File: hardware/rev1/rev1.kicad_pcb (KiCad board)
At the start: 2 copper layers, 26 parts, among them U1 BNO055, U2 MPL3115A2, U3 Teensy3.6, Y1 Crystal_32kHz768

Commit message: wip
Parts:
- moved Y1 168.0 mm to (132.1, 140.7), turned to 90 degrees
- moved C1 166.6 mm to (132.6, 146.4)
- moved C2 165.9 mm to (132.6, 142.6), turned to 180 degrees
- moved C3 164.3 mm to (132.6, 144.5), turned to 180 degrees
- moved C5 157.1 mm to (135.3, 140.6)
- moved R2 155.9 mm to (128.3, 143.4), turned to 180 degrees
- moved R3 155.0 mm to (131.6, 135.6), turned to 180 degrees
- moved C4 154.7 mm to (125.6, 141.6), turned to 270 degrees
- moved C6 152.6 mm to (135.3, 138.4)
- moved TP6 151.5 mm to (124.2, 135.8)
- moved R1 147.6 mm to (125.0, 138.7)
- moved R4 144.7 mm to (128.3, 135.6)
- moved TP_GND1 143.5 mm to (120.7, 135.6)
- moved TP7 143.2 mm to (116.6, 135.6)
- moved TP3 138.9 mm to (122.8, 141.7)
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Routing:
- net OptionalOSCoutput: track 0.00 -> 3.06 mm
- net OptionalOSCinput: track 0.00 -> 1.88 mm
- net VDD: track 0.00 -> 1.63 mm

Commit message: wip
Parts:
- added TP10: TestPoint, footprints:Test_Point_D1.02mm, F.Cu at (135.4, 135.5)
- added TP9: TestPoint, footprints:Test_Point_D1.02mm, F.Cu at (136.2, 143.2)
- moved TP6 4.32 mm to (119.9, 135.6)
- moved TP_GND1 4.25 mm to (116.4, 135.6)
- moved TP7 3.75 mm to (112.8, 135.6)
- moved TP3 0.40 mm to (122.9, 141.3)
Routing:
- net GND: track 0.00 -> 19.0 mm
- net nBOOT_LOAD_PIN: track 0.00 -> 15.9 mm, vias 0 -> 1
- net nRESET: track 0.00 -> 6.56 mm, vias 0 -> 1
- net VDD: track 1.63 -> 7.65 mm
- net OptionalOSCoutput: track 3.06 -> 8.73 mm
- net OptionalOSCinput: track 1.88 -> 7.52 mm
- net Net-(C4-Pad1): track 0.00 -> 4.58 mm
- net INT_BNO055: track 0.00 -> 4.49 mm, vias 0 -> 1

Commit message: wip (slick)
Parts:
- moved R3 0.97 mm to (131.8, 134.7)
- moved R4 0.96 mm to (128.4, 134.7)
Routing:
- net VDD: track 7.65 -> 32.7 mm, vias 0 -> 3
- net COM3: track 0.00 -> 5.26 mm, vias 0 -> 1
- net SDA_TEENSY: track 0.00 -> 5.03 mm
- net SCL_TEENSY: track 0.00 -> 4.72 mm
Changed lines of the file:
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@@
     (thickness 1.6)
     (drawings 0)
-    (tracks 73)
+    (tracks 107)
     (zones 0)
     (modules 28)
@@
   )
   (module footprints:R_0805_OEM (layer F.Cu)
-    (at 131.572 135.636 180)
+    (at 131.7625 134.6835 180)
     (descr "Resistor SMD 0805, reflow soldering, Vishay (see dcrcw.pdf)")
     (tags "resistor 0805")
@@
   )
   (module footprints:R_0805_OEM (layer F.Cu)
-    (at 128.27 135.636)
+    (at 128.397 134.6835)
     (descr "Resistor SMD 0805, reflow soldering, Vishay (see dcrcw.pdf)")
     (tags "resistor 0805")
@@
   (segment (start 129.22 143.1265) (end 128.906 142.8125) (width 0.25) (layer F.Cu) (net 2) (status C00000))
   (segment (start 128.906 142.8125) (end 128.906 141.8185) (width 0.25) (layer F.Cu) (net 2) (status C00000))
+  (segment (start 127.447 134.6835) (end 127.447 136.078) (width 0.25) (layer F.Cu) (net 2) (status 400000))
+  (segment (start 127.3175 137.287) (end 130.3655 140.335) (width 0.25) (layer B.Cu) (net 2))
+  (segment (start 127.3175 137.16) (end 127.3175 137.287) (width 0.25) (layer B.Cu) (net 2))
+  (segment (start 127.447 136.078) (end 127.3175 136.2075) (width 0.25) (layer F.Cu) (net 2))
+  (via (at 127.3175 136.2075) (size 0.8) (drill 0.4) (layers F.Cu B.Cu) (net 2))
+  (segment (start 127.3175 136.2075) (end 127.3175 137.16) (width 0.25) (layer B.Cu) (net 2))
+  (segment (start 132.7125 134.6835) (end 132.7125 134.8765) (width 0.25) (layer F.Cu) (net 2) (status C00000))
+  (segment (start 130.3655 139.319) (end 130.3655 137.2235) (width 0.25) (layer B.Cu) (net 2))
+  (segment (start 130.3655 142.748) (end 130.3655 140.335) (width 0.25) (layer B.Cu) (net 2))
+  (segment (start 130.3655 140.335) (end 130.3655 139.319) (width 0.25) (layer B.Cu) (net 2))
+  (via (at 130.3655 142.748) (size 0.8) (drill 0.4) (layers F.Cu B.Cu) (net 2))
+  (segment (start 129.7305 142.748) (end 130.3655 142.748) (width 0.25) (layer F.Cu) (net 2))
+  (segment (start 129.22 143.2585) (end 129.7305 142.748) (width 0.25) (layer F.Cu) (net 2) (status 400000))
+  (segment (start 129.22 143.2585) (end 129.22 143.383) (width 0.25) (layer F.Cu) (net 2) (status C00000))
+  (segment (start 132.7125 134.8765) (end 131.3815 136.2075) (width 0.25) (layer F.Cu) (net 2) (status 400000))
+  (via (at 131.3815 136.2075) (size 0.8) (drill 0.4) (layers F.Cu B.Cu) (net 2))
+  (segment (start 131.3815 136.2075) (end 130.3655 137.2235) (width 0.25) (layer B.Cu) (net 2))
+  (segment (start 124.018 138.684) (end 124.018 136.586) (width 0.25) (layer F.Cu) (net 2) (status 400000))
+  (segment (start 125.9205 134.6835) (end 127.447 134.6835) (width 0.25) (layer F.Cu) (net 2) (status 800000))
+  (segment (start 124.018 136.586) (end 125.9205 134.6835) (width 0.25) (layer F.Cu) (net 2))
+  (segment (start 130.3655 142.748) (end 131.461 142.748) (width 0.25) (layer F.Cu) (net 2) (status 800000))
+  (segment (start 131.461 142.748) (end 131.588 142.621) (width 0.25) (layer F.Cu) (net 2) (status C00000))
   (segment (start 127.0935 140.256) (end 125.952 140.256) (width 0.25) (layer F.Cu) (net 3) (status C00000))
   (segment (start 125.952 140.256) (end 125.603 140.605) (width 0.25) (layer F.Cu) (net 3) (status C00000))
@@
   (segment (start 124.206 142.748) (end 124.9045 142.0495) (width 0.25) (layer B.Cu) (net 8))
   (segment (start 124.9045 142.0495) (end 124.9045 139.7635) (width 0.25) (layer B.Cu) (net 8))
+  (segment (start 130.2185 137.256) (end 130.2185 135.2775) (width 0.25) (layer F.Cu) (net 9) (status 400000))
+  (segment (start 130.2185 135.2775) (end 130.8125 134.6835) (width 0.25) (layer F.Cu) (net 9) (status 800000))
+  (segment (start 130.8125 134.6835) (end 130.8125 132.649) (width 0.25) (layer F.Cu) (net 9) (status 400000))
+  (segment (start 130.8125 132.649) (end 130.937 132.5245) (width 0.25) (layer F.Cu) (net 9))
+  (segment (start 129.406 137.1935) (end 129.406 134.7425) (width 0.25) (layer F.Cu) (net 10) (status C00000))
+  (segment (start 129.406 134.7425) (end 129.347 134.6835) (width 0.25) (layer F.Cu) (net 10) (status C00000))
+  (segment (start 129.347 134.6835) (end 129.347 132.5855) (width 0.25) (layer F.Cu) (net 10) (status 400000))
+  (segment (start 129.347 132.5855) (end 129.286 132.5245) (width 0.25) (layer F.Cu) (net 10))
+  (segment (start 128.406 137.1935) (end 128.406 136.262) (width 0.25) (layer F.Cu) (net 13) (status 400000))
+  (segment (start 128.4605 136.2075) (end 128.4605 131.953) (width 0.25) (layer B.Cu) (net 13))
+  (via (at 128.4605 136.2075) (size 0.8) (drill 0.4) (layers F.Cu B.Cu) (net 13))
+  (segment (start 128.406 136.262) (end 128.4605 136.2075) (width 0.25) (layer F.Cu) (net 13))
   (segment (start 127.0935 137.756) (end 126.7705 137.756) (width 0.25) (layer F.Cu) (net 14) (status 400000))
   (segment (start 126.111 137.0965) (end 126.111 133.858) (width 0.25) (layer B.Cu) (net 14))

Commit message: wip
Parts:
- moved R2 1.38 mm to (128.3, 144.8)
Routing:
- net GND: track 19.0 -> 60.3 mm, vias 0 -> 6
- net VDD: track 32.7 -> 40.6 mm
- net INT_BNO055: track 4.49 -> 1.26 mm
- net nBOOT_LOAD_PIN: track 15.9 -> 17.2 mm

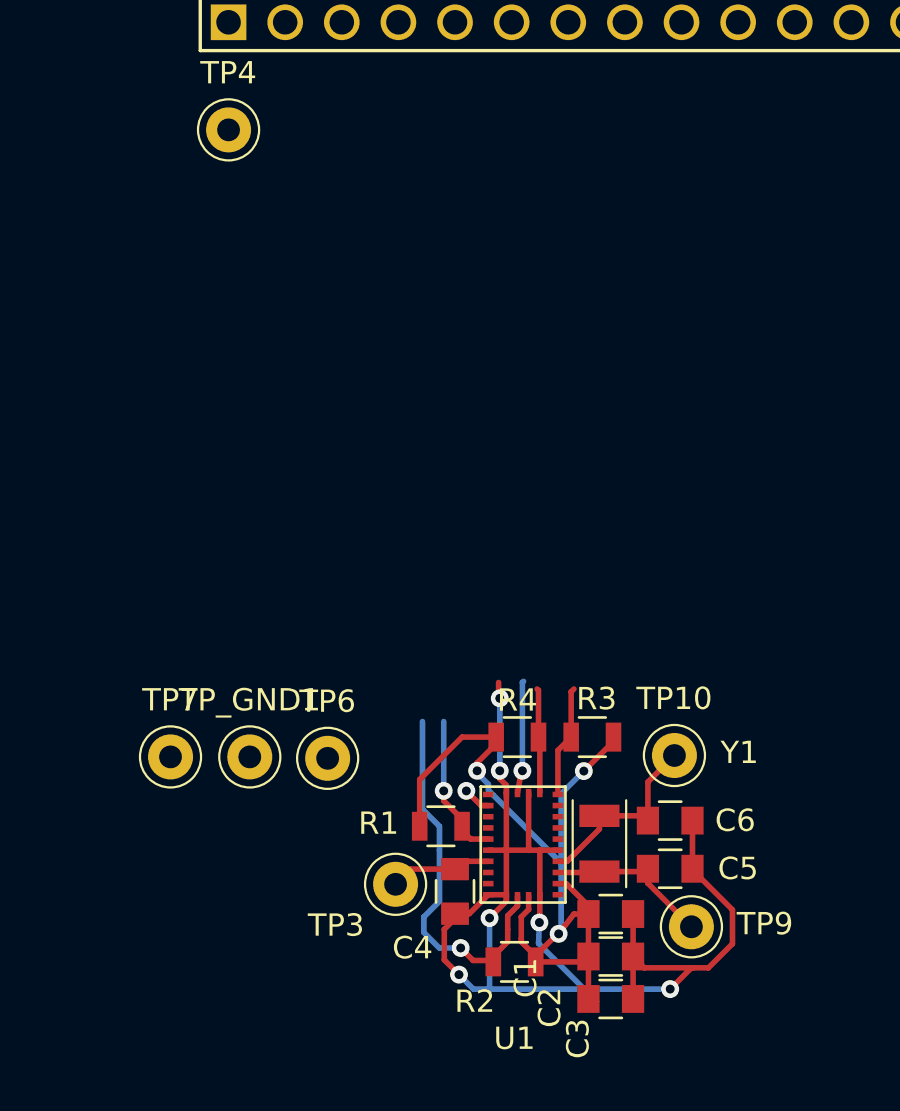
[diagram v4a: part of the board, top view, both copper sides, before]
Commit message: finish BNO055 portion of layout
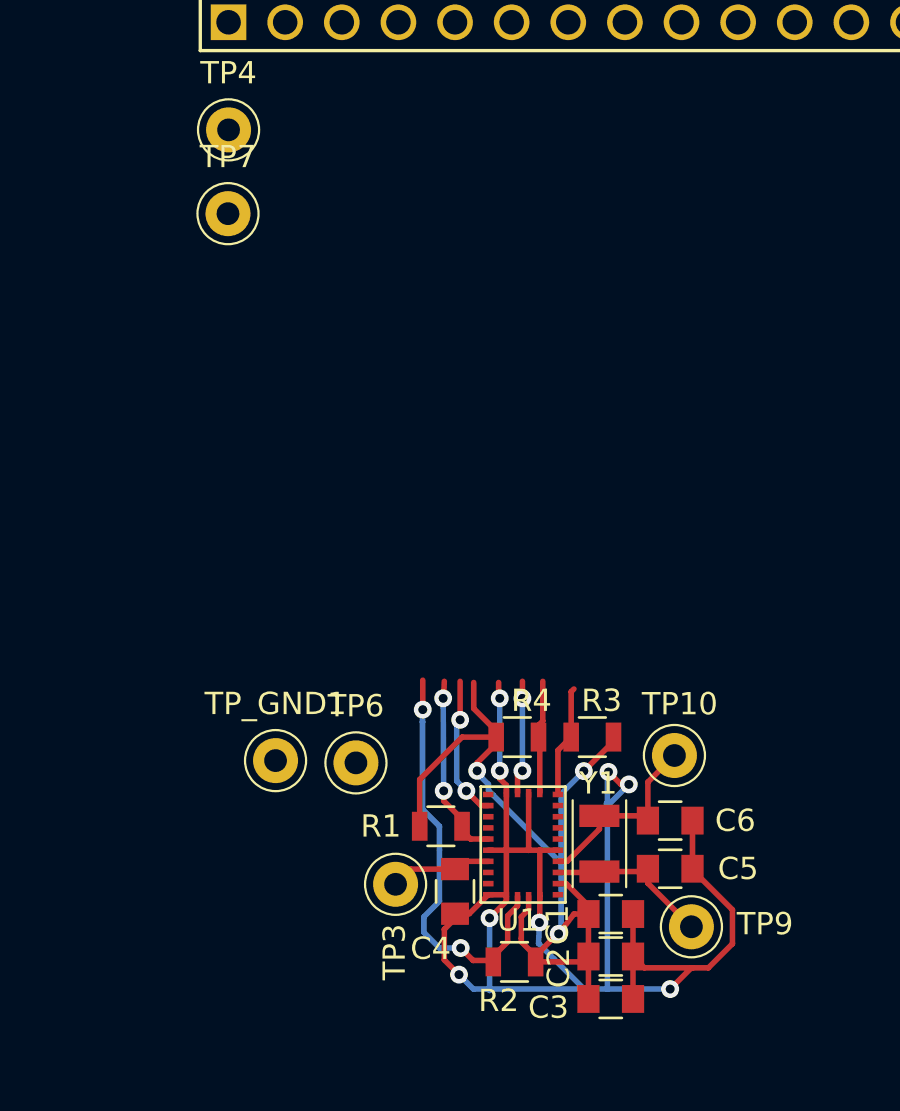
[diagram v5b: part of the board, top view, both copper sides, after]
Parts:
- moved TP7 24.5 mm to (115.4, 111.2)
- moved TP6 1.29 mm to (121.2, 135.8)
- moved TP_GND1 1.17 mm to (117.6, 135.7)
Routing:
- net GND: track 60.3 -> 72.3 mm, vias 6 -> 8
- net INT_BNO055: track 1.26 -> 6.41 mm, vias 1 -> 2
- net VDD: track 40.6 -> 43.5 mm
- net nBOOT_LOAD_PIN: track 17.2 -> 19.1 mm, vias 1 -> 2
- net nRESET: track 6.56 -> 8.40 mm, vias 1 -> 2
- net COM3: track 5.07 -> 5.18 mm, vias 1 -> 2

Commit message: wip
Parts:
- moved U2 188.1 mm to (159.7, 137.6)
- moved TP8 182.6 mm to (167.4, 139.0)
- moved C9 179.9 mm to (163.4, 137.3)
- moved C7 138.2 mm to (163.4, 135.3)
- moved TP1 132.3 mm to (117.6, 132.0)
- moved TP2 132.1 mm to (121.2, 132.0)
- moved C8 120.3 mm to (163.4, 133.3), turned to 0 degrees
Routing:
- net VDD: track 43.5 -> 59.9 mm, vias 3 -> 5
- net GND: track 72.3 -> 82.5 mm
- net nRESET: track 8.40 -> 17.1 mm
- net Net-(C9-Pad1): track 0.00 -> 7.95 mm, vias 0 -> 1
- net nBOOT_LOAD_PIN: track 19.1 -> 20.6 mm
